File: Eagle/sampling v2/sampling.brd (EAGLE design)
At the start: 54.3 x 38.1 mm, 8 parts, among them X1 JST-XH-04-PIN-LONG-PAD

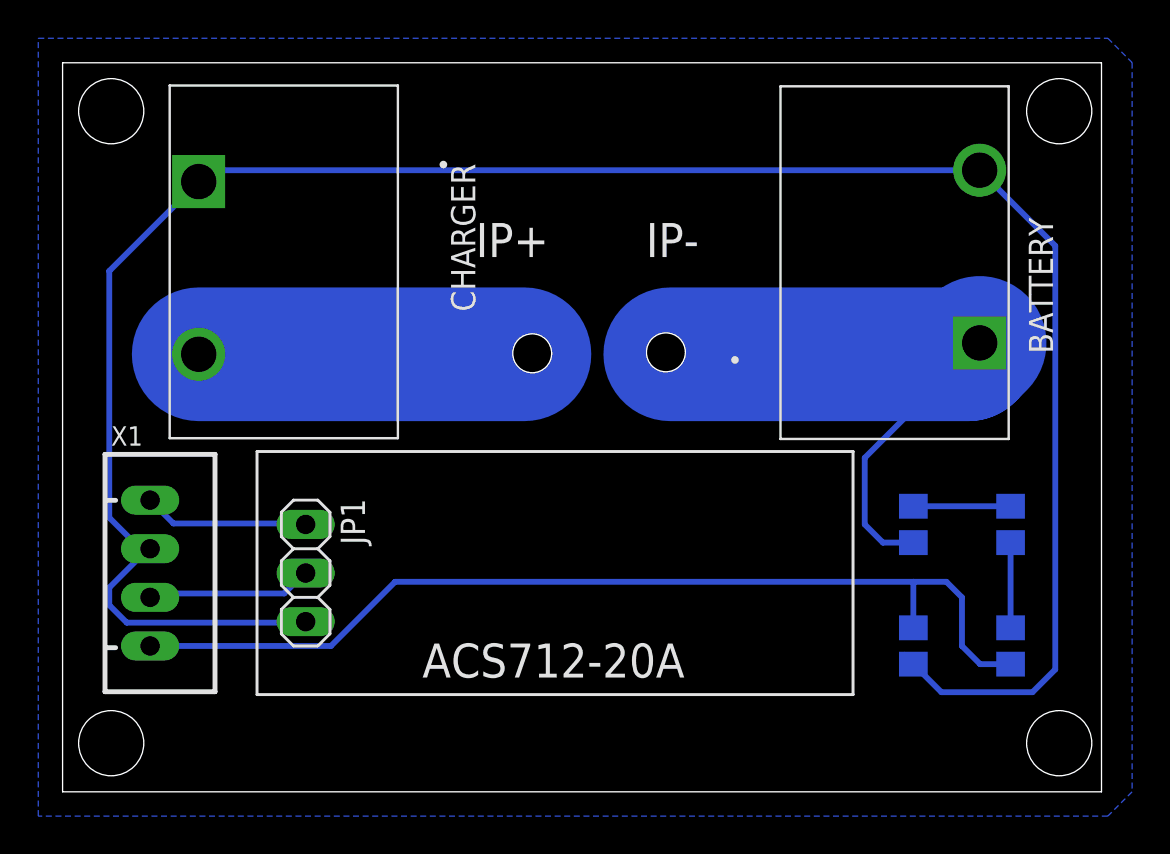
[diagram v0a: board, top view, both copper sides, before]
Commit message: update sampling board
zener, divider HV, update divider batt
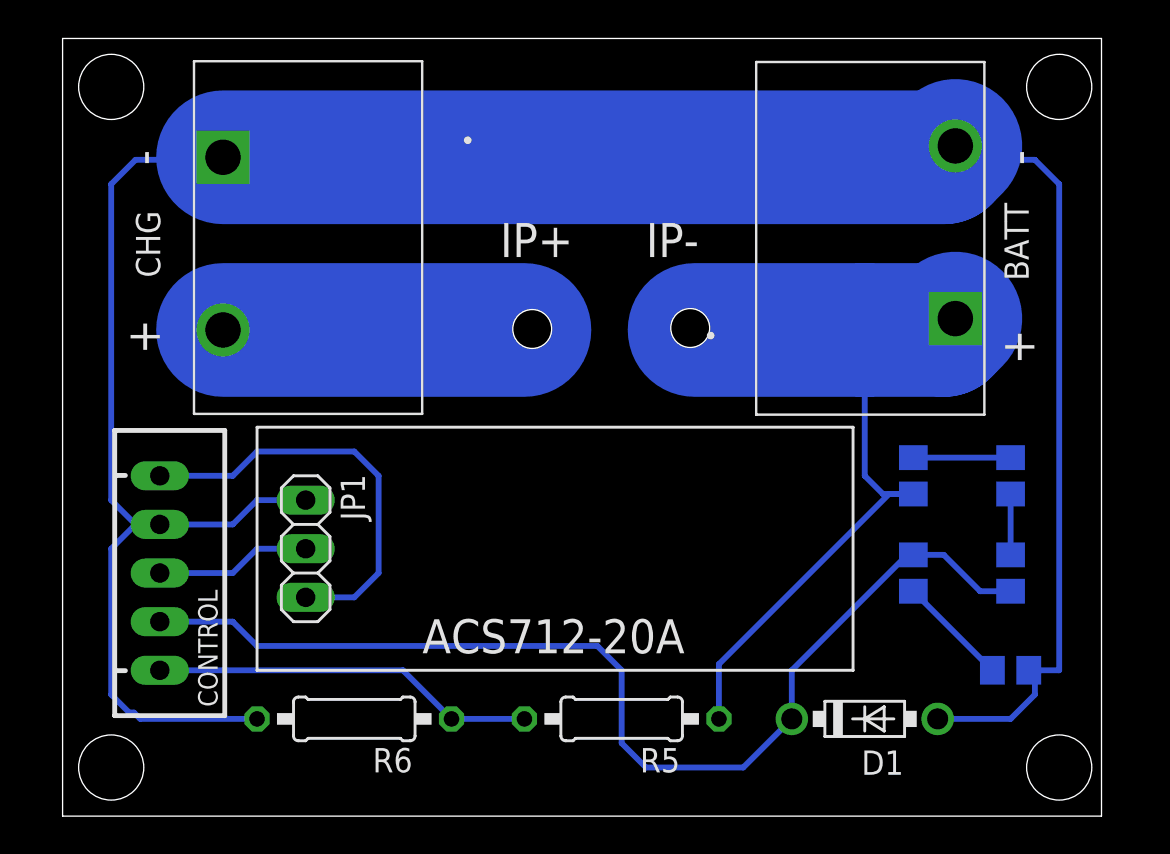
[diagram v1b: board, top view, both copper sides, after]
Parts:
- removed BATTERY, CHARGER: 1977477-2, terminal_block_TA:TE_1977477-2
- removed X1: JST-XH-04-PIN-LONG-PAD, Rembrandt Electronics - JST XH Connectors v1-0:JST-XH-04-PACKAGE-LONG-PAD
- added BATT, CHG: 1977477-2, terminal_block_TA:TE_1977477-2
- added CONTROL: JST-XH-05-PIN-LONG-PAD, Rembrandt Electronics - JST XH Connectors v1-0:JST-XH-05-PACKAGE-LONG-PAD
- added D1: 1N5817-B, diode:DO41-7.6
- added R5: 680k, rcl:0207/10
- added R6: 10k, rcl:0207/10
- added R7: 100k, rcl:R0805
- moved R1 3.81 mm to (49.5, 11.4)
- moved R2 3.81 mm to (44.5, 11.4)
- moved R3 2.54 mm to (49.5, 16.5)
- moved R4 2.54 mm to (44.5, 16.5)
- moved JP1 1.27 mm to (12.7, 12.7)
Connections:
- new net HV_SENSE: CONTROL.5, R5.2, R6.1
- new net N$3: R2.1, R7.2
- net 5V: now also CONTROL.1, JP1.3; no longer JP1.1, X1.1
- net CURRENT_SENSE: now also CONTROL.3; no longer X1.3
- net GND: now also BATT.2, CHG.1, CONTROL.2, D1.A, JP1.1, R6.2, R7.1; no longer BATTERY.2, CHARGER.1, JP1.3, R2.1, X1.2
- net VIN: now also CHG.2; no longer CHARGER.2
- net VOLTAGE_SENSE: now also CONTROL.4, D1.C; no longer X1.4
- net VOUT: now also BATT.1, R5.1; no longer BATTERY.1
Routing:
- net HV_SENSE: track 0.00 -> 20.1 mm
- net GND: track 115.1 -> 130.3 mm
- net 5V: track 8.64 -> 21.9 mm
- net VOUT: track 32.6 -> 42.4 mm
- net N$3: track 0.00 -> 5.84 mm
- net VOLTAGE_SENSE: track 52.0 -> 56.7 mm
- net VIN: track 17.0 -> 15.7 mm
- net N$1: track 4.45 -> 3.18 mm
- net CURRENT_SENSE: track 8.76 -> 8.15 mm
- removed copper zone on layer 16, net GND
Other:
- board size 54.3 x 38.1 mm -> 54.3 x 40.6 mm
- board text added: "+"
- board text added: "-"
